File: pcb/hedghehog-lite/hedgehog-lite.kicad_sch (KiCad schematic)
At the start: 31 parts, among them J1 Conn_01x04, J2 AVR-ISP-6, SW1 Reset, SW2 HWB, U1 ATmega32U4-M, Y1 16MHz

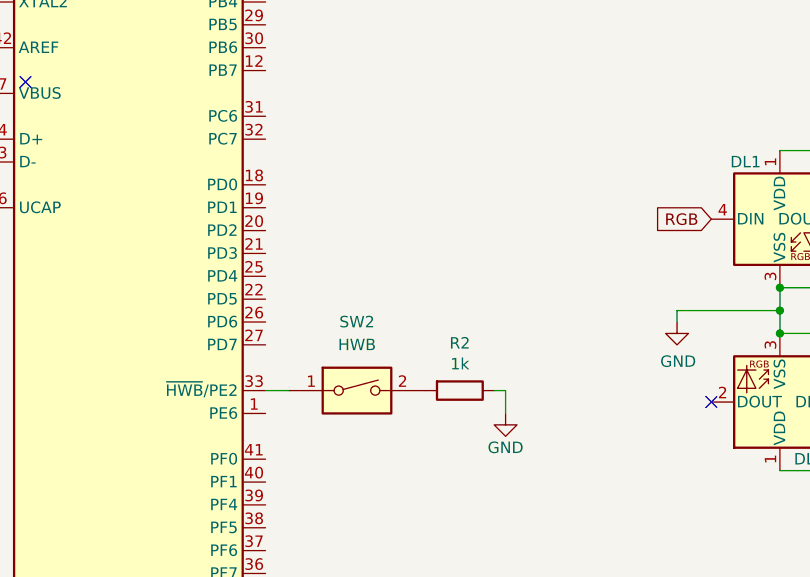
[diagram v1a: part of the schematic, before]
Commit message: Placed all components on PCB
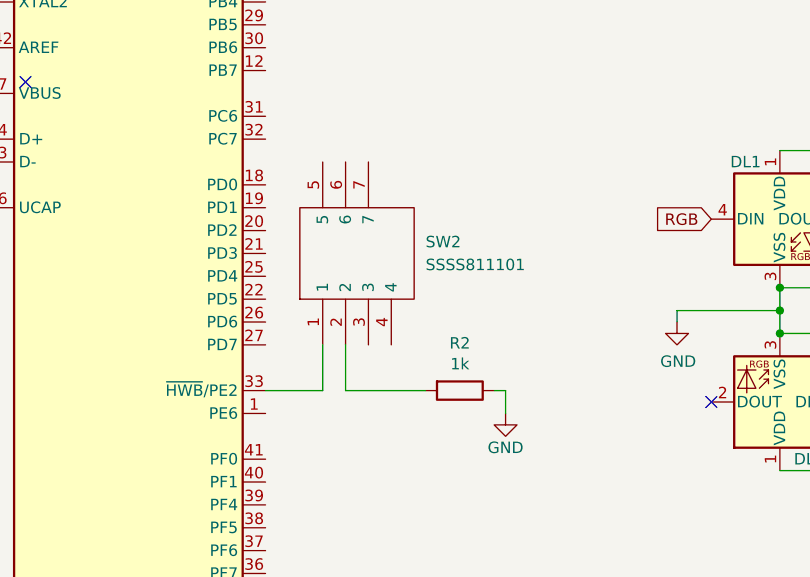
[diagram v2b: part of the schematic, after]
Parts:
- removed SW2: HWB, Button_Switch_SMD:SW_DIP_SPSTx01_Slide_6.7x4.1mm_W8.61mm_P2.54mm_LowProfile, symbol Switch:SW_DIP_x01
- added SW2: SSSS811101, SSSS811101:SSSS811101, symbol SSSS811101:SSSS811101
- DL1, DL10, DL11, DL12, DL13, DL14, DL15, DL2, DL3, DL4, DL5, DL6, DL7, DL8, DL9: LCSC Part # (none) -> C2874885
- J1: LCSC Part # (none) -> C160404
- U1: LCSC Part # (none) -> C112161
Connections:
- net at U1.33 (~{HWB}/PE2): now also SW2.1
- net at R2.2: now also SW2.2

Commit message: Wiring up all parts, excluding matrix
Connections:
- net +5V: no longer DL10.1 (VDD), DL11.1 (VDD), DL12.1 (VDD), DL13.1 (VDD), DL14.1 (VDD), DL15.1 (VDD), DL8.1 (VDD), DL9.1 (VDD)
- net LED_PWR_P: now also DL10.1 (VDD), DL11.1 (VDD), DL12.1 (VDD), DL13.1 (VDD), DL14.1 (VDD), DL15.1 (VDD), DL8.1 (VDD), DL9.1 (VDD)
- net RGB: now also U1.41 (PF0)
- no-connect marks 3 -> 8
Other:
- note added: "Underglow LEDs can be added or left without power. Leave them off during initial flash to reduce ISP current"
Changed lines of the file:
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@@
   (junction (at 77.47 73.66) (diameter 0) (color 0 0 0 0)
   )
+  (no_connect (at 92.71 86.36))
+  (no_connect (at 106.68 134.62))
+  (no_connect (at 104.14 114.3))
+  (no_connect (at 101.6 114.3))
+  (no_connect (at 104.14 134.62))
   (no_connect (at 62.23 101.6))
-  (no_connect (at 66.04 105.41))
+  (no_connect (at 99.06 114.3))
   (no_connect (at 142.24 140.97))
   (wire (pts (xy 256.54 21.59) (xy 264.16 21.59))
@@
     (stroke (width 0) (type default) (color 0 0 0 0))
   )
+  (polyline (pts (xy 217.17 48.26) (xy 278.13 48.26))
+    (stroke (width 0) (type default) (color 0 0 0 0))
+  )
   (wire (pts (xy 46.99 39.37) (xy 57.15 39.37))
     (stroke (width 0) (type default) (color 0 0 0 0))
@@
     (stroke (width 0) (type default) (color 0 0 0 0))
   )
+  (polyline (pts (xy 217.17 48.26) (xy 217.17 57.15))
+    (stroke (width 0) (type default) (color 0 0 0 0))
+  )
   (wire (pts (xy 180.34 128.27) (xy 195.58 128.27))
     (stroke (width 0) (type default) (color 0 0 0 0))
@@
     (stroke (width 0) (type default) (color 0 0 0 0))
   )
+  (wire (pts (xy 92.71 147.32) (xy 101.6 147.32))
+    (stroke (width 0) (type default) (color 0 0 0 0))
+  )
   (wire (pts (xy 149.86 130.81) (xy 138.43 130.81))
     (stroke (width 0) (type default) (color 0 0 0 0))
@@
     (stroke (width 0) (type default) (color 0 0 0 0))
   )
+  (polyline (pts (xy 278.13 48.26) (xy 278.13 57.15))
+    (stroke (width 0) (type default) (color 0 0 0 0))
+  )
   (wire (pts (xy 259.08 25.4) (xy 264.16 25.4))
     (stroke (width 0) (type default) (color 0 0 0 0))
@@
     (stroke (width 0) (type default) (color 0 0 0 0))
   )
+  (polyline (pts (xy 278.13 57.15) (xy 217.17 57.15))
+    (stroke (width 0) (type default) (color 0 0 0 0))
+  )
   (wire (pts (xy 241.3 148.59) (xy 256.54 148.59))
     (stroke (width 0) (type default) (color 0 0 0 0))
@@
   (wire (pts (xy 46.99 35.56) (xy 46.99 39.37))
     (stroke (width 0) (type default) (color 0 0 0 0))
+  )
+  (text "Underglow LEDs can be added or left without power. Leave\nthem off during initial flash to reduce ISP current"
+    (at 218.44 53.34 0)
+    (effects (font (size 1.27 1.27)) (justify left bottom))
   )
   (global_label "SCK" (shape input) (at 100.33 88.9 0) (fields_autoplaced)
@@
     )
   )
-  (global_label "LED_PWR_P" (shape input) (at 187.96 105.41 90) (fields_autoplaced)
+  (global_label "LED_PWR_P" (shape input) (at 187.96 105.41 0) (fields_autoplaced)
     (effects (font (size 1.27 1.27)) (justify left))
-    (property "Intersheet References" "${INTERSHEET_REFS}" (id 0) (at 187.8806 92.3531 90)
+    (property "Intersheet References" "${INTERSHEET_REFS}" (id 0) (at 201.0169 105.3306 0)
+      (effects (font (size 1.27 1.27)) (justify left) hide)
+    )
+  )
+  (global_label "LED_PWR_P" (shape input) (at 203.2 152.4 0) (fields_autoplaced)
+    (effects (font (size 1.27 1.27)) (justify left))
+    (property "Intersheet References" "${INTERSHEET_REFS}" (id 0) (at 216.2569 152.3206 0)
       (effects (font (size 1.27 1.27)) (justify left) hide)
     )
@@
     (property "Intersheet References" "${INTERSHEET_REFS}" (id 0) (at 40.7669 111.6806 0)
       (effects (font (size 1.27 1.27)) (justify right) hide)
+    )
+  )
+  (global_label "RGB" (shape input) (at 101.6 147.32 0) (fields_autoplaced)
+    (effects (font (size 1.27 1.27)) (justify left))
+    (property "Intersheet References" "${INTERSHEET_REFS}" (id 0) (at 107.8231 147.3994 0)
+      (effects (font (size 1.27 1.27)) (justify left) hide)
     )
   )
@@
     (pin "3")
     (pin "4")
-  )
-  (symbol (lib_id "power:VCC") (at 203.2 152.4 180) (unit 1)
-    (in_bom yes) (on_board yes)
-    (property "Reference" "#PWR0121" (id 0) (at 203.2 148.59 0)
-      (effects (font (size 1.27 1.27)) hide)
-    )
-    (property "Value" "VCC" (id 1) (at 205.74 153.6699 0)
-      (effects (font (size 1.27 1.27)) (justify right))
-    )
-    (property "Footprint" "" (id 2) (at 203.2 152.4 0)
-      (effects (font (size 1.27 1.27)) hide)
-    )
-    (property "Datasheet" "" (id 3) (at 203.2 152.4 0)
-      (effects (font (size 1.27 1.27)) hide)
-    )
-    (pin "1")
   )
   (symbol (lib_id "LED:WS2812B") (at 241.3 120.65 0) (unit 1)
@@
     (pin "1")
   )
-  (sheet (at 139.7 59.69) (size 93.98 29.21) (fields_autoplaced)
+  (sheet (at 113.03 55.88) (size 93.98 29.21) (fields_autoplaced)
     (stroke (width 0.1524) (type solid) (color 0 0 0 0))
     (fill (color 0 0 0 0.0000))
-    (property "Sheet name" "Switch Matrix" (id 0) (at 139.7 58.9784 0)
+    (property "Sheet name" "Switch Matrix" (id 0) (at 113.03 55.1684 0)
       (effects (font (size 1.27 1.27)) (justify left bottom))
     )
-    (property "Sheet file" "sw_matrix.kicad_sch" (id 1) (at 139.7 89.4846 0)
+    (property "Sheet file" "sw_matrix.kicad_sch" (id 1) (at 113.03 85.6746 0)
       (effects (font (size 1.27 1.27)) (justify left top))
     )
@@
       (reference "#PWR0120") (unit 1) (value "GND") (footprint "")
     )
-    (path "/7712bc7a-4dd6-4ab1-86d1-22dc5a419cde"
-      (reference "#PWR0121") (unit 1) (value "VCC") (footprint "")
-    )
     (path "/421acd2a-e010-4147-aed0-31f70fcce876"

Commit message: all done but switches
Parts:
- added R3, R4: 22, Resistor_SMD:R_0805_2012Metric, symbol bakeneko-60-pcb-rescue:R-Device
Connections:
- net DN: now also R4.2; no longer U1.3 (D-)
- net DP: now also R3.2; no longer U1.4 (D+)
- new net: R3.1, U1.4 (D+)
- new net: R4.1, U1.3 (D-)
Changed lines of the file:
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@@
   (junction (at 153.67 26.67) (diameter 0) (color 0 0 0 0)
-  )
-  (junction (at 243.84 21.59) (diameter 0) (color 0 0 0 0)
   )
   (junction (at 165.1 148.59) (diameter 0) (color 0 0 0 0)
@@
     (stroke (width 0) (type default) (color 0 0 0 0))
   )
-  (wire (pts (xy 238.76 21.59) (xy 243.84 21.59))
+  (wire (pts (xy 238.76 21.59) (xy 248.92 21.59))
     (stroke (width 0) (type default) (color 0 0 0 0))
   )
@@
     (stroke (width 0) (type default) (color 0 0 0 0))
   )
+  (wire (pts (xy 34.29 110.49) (xy 38.1 110.49))
+    (stroke (width 0) (type default) (color 0 0 0 0))
+  )
   (polyline (pts (xy 217.17 48.26) (xy 278.13 48.26))
     (stroke (width 0) (type default) (color 0 0 0 0))
@@
     (stroke (width 0) (type default) (color 0 0 0 0))
   )
+  (wire (pts (xy 34.29 114.3) (xy 38.1 114.3))
+    (stroke (width 0) (type default) (color 0 0 0 0))
+  )
   (wire (pts (xy 99.06 139.7) (xy 99.06 134.62))
     (stroke (width 0) (type default) (color 0 0 0 0))
@@
     (stroke (width 0) (type default) (color 0 0 0 0))
   )
+  (wire (pts (xy 45.72 110.49) (xy 45.72 111.76))
+    (stroke (width 0) (type default) (color 0 0 0 0))
+  )
   (wire (pts (xy 119.38 142.24) (xy 119.38 139.7))
     (stroke (width 0) (type default) (color 0 0 0 0))
@@
   )
   (wire (pts (xy 36.83 24.13) (xy 46.99 24.13))
-    (stroke (width 0) (type default) (color 0 0 0 0))
-  )
-  (wire (pts (xy 243.84 21.59) (xy 248.92 21.59))
     (stroke (width 0) (type default) (color 0 0 0 0))
   )
@@
     )
   )
-  (global_label "DN" (shape input) (at 45.72 114.3 180) (fields_autoplaced)
+  (global_label "DN" (shape input) (at 34.29 114.3 180) (fields_autoplaced)
     (effects (font (size 1.27 1.27)) (justify right))
-    (property "Intersheet References" "${INTERSHEET_REFS}" (id 0) (at 40.7064 114.2206 0)
+    (property "Intersheet References" "${INTERSHEET_REFS}" (id 0) (at 29.2764 114.2206 0)
       (effects (font (size 1.27 1.27)) (justify right) hide)
     )
@@
     )
   )
-  (global_label "DP" (shape input) (at 45.72 111.76 180) (fields_autoplaced)
+  (global_label "DP" (shape input) (at 34.29 110.49 180) (fields_autoplaced)
     (effects (font (size 1.27 1.27)) (justify right))
-    (property "Intersheet References" "${INTERSHEET_REFS}" (id 0) (at 40.7669 111.6806 0)
+    (property "Intersheet References" "${INTERSHEET_REFS}" (id 0) (at 29.3369 110.4106 0)
       (effects (font (size 1.27 1.27)) (justify right) hide)
     )
@@
     (pin "1")
   )
+  (symbol (lib_id "bakeneko-60-pcb-rescue:R-Device") (at 41.91 110.49 270) (unit 1)
+    (in_bom yes) (on_board yes)
+    (property "Reference" "R3" (id 0) (at 41.91 108.585 90))
+    (property "Value" "22" (id 1) (at 41.91 110.49 90))
+    (property "Footprint" "Resistor_SMD:R_0805_2012Metric" (id 2) (at 41.91 108.712 90)
+      (effects (font (size 1.27 1.27)) hide)
+    )
+    (property "Datasheet" "~" (id 3) (at 41.91 110.49 0)
+      (effects (font (size 1.27 1.27)) hide)
+    )
+    (property "LCSC Part #" "C17561" (id 4) (at 41.91 110.49 0)
+      (effects (font (size 1.27 1.27)) hide)
+    )
+    (pin "1")
+    (pin "2")
+  )
   (symbol (lib_id "bakeneko-60-pcb-rescue:Crystal_GND24-Device") (at 95.25 31.75 90) (unit 1)
     (in_bom yes) (on_board yes)
@@
     )
     (property "LCSC Part #" "C15850" (id 4) (at 57.15 31.75 0)
+      (effects (font (size 1.27 1.27)) hide)
+    )
+    (pin "1")
+    (pin "2")
+  )
+  (symbol (lib_id "bakeneko-60-pcb-rescue:R-Device") (at 41.91 114.3 270) (unit 1)
+    (in_bom yes) (on_board yes)
+    (property "Reference" "R4" (id 0) (at 41.91 112.395 90))
+    (property "Value" "22" (id 1) (at 41.91 114.3 90))
+    (property "Footprint" "Resistor_SMD:R_0805_2012Metric" (id 2) (at 41.91 112.522 90)
+      (effects (font (size 1.27 1.27)) hide)
+    )
+    (property "Datasheet" "~" (id 3) (at 41.91 114.3 0)
+      (effects (font (size 1.27 1.27)) hide)
+    )
+    (property "LCSC Part #" "C17561" (id 4) (at 41.91 114.3 0)
       (effects (font (size 1.27 1.27)) hide)
     )
@@
     (pin "2")
   )
-  (symbol (lib_id "power:VBUS") (at 256.54 21.59 0) (unit 1)
-    (in_bom yes) (on_board yes) (fields_autoplaced)
-    (property "Reference" "#PWR0114" (id 0) (at 256.54 25.4 0)
-      (effects (font (size 1.27 1.27)) hide)
-    )
-    (property "Value" "VBUS" (id 1) (at 256.54 16.51 0))
-    (property "Footprint" "" (id 2) (at 256.54 21.59 0)
-      (effects (font (size 1.27 1.27)) hide)
-    )
-    (property "Datasheet" "" (id 3) (at 256.54 21.59 0)
-      (effects (font (size 1.27 1.27)) hide)
-    )
-    (pin "1")
-  )
   (symbol (lib_id "Connector_Generic:Conn_01x04") (at 269.24 25.4 0) (unit 1)
     (in_bom yes) (on_board yes) (fields_autoplaced)
@@
     (pin "1")
   )
-  (symbol (lib_id "power:VBUS") (at 243.84 21.59 0) (unit 1)
-    (in_bom yes) (on_board yes) (fields_autoplaced)
-    (property "Reference" "#PWR0112" (id 0) (at 243.84 25.4 0)
-      (effects (font (size 1.27 1.27)) hide)
-    )
-    (property "Value" "VBUS" (id 1) (at 243.84 16.51 0))
-    (property "Footprint" "" (id 2) (at 243.84 21.59 0)
-      (effects (font (size 1.27 1.27)) hide)
-    )
-    (property "Datasheet" "" (id 3) (at 243.84 21.59 0)
-      (effects (font (size 1.27 1.27)) hide)
-    )
-    (pin "1")
-  )
   (symbol (lib_id "LED:WS2812B") (at 256.54 140.97 180) (unit 1)
     (in_bom yes) (on_board yes)
@@
     (pin "3")
     (pin "4")
+  )
+  (symbol (lib_id "power:VCC") (at 256.54 21.59 0) (unit 1)
+    (in_bom yes) (on_board yes)
+    (property "Reference" "#PWR0112" (id 0) (at 256.54 25.4 0)
+      (effects (font (size 1.27 1.27)) hide)
+    )
+    (property "Value" "VCC" (id 1) (at 256.54 16.51 0))
+    (property "Footprint" "" (id 2) (at 256.54 21.59 0)
+      (effects (font (size 1.27 1.27)) hide)
+    )
+    (property "Datasheet" "" (id 3) (at 256.54 21.59 0)
+      (effects (font (size 1.27 1.27)) hide)
+    )
+    (pin "1")
   )
   (symbol (lib_id "LED:WS2812B") (at 241.3 140.97 180) (unit 1)
@@
     (pin "1")
   )
-  (sheet (at 113.03 55.88) (size 93.98 29.21) (fields_autoplaced)
+  (sheet (at 113.03 57.15) (size 39.37 27.94) (fields_autoplaced)
     (stroke (width 0.1524) (type solid) (color 0 0 0 0))
     (fill (color 0 0 0 0.0000))
-    (property "Sheet name" "Switch Matrix" (id 0) (at 113.03 55.1684 0)
+    (property "Sheet name" "Switch Matrix" (id 0) (at 113.03 56.4384 0)
       (effects (font (size 1.27 1.27)) (justify left bottom))
     )
@@
       (reference "#PWR0111") (unit 1) (value "VCC") (footprint "")
     )
-    (path "/a993c56f-11f6-4404-bd64-e97c4f8902c7"
-      (reference "#PWR0112") (unit 1) (value "VBUS") (footprint "")
+    (path "/dad34091-c7fa-46ac-8890-1f6569d146a1"
+      (reference "#PWR0112") (unit 1) (value "VCC") (footprint "")
     )
     (path "/38bc573d-ed33-43d3-b37e-dbdc7be602cb"
       (reference "#PWR0113") (unit 1) (value "+5V") (footprint "")
     )
-    (path "/979634cd-c88e-45a9-a703-4310b6d115d4"
-      (reference "#PWR0114") (unit 1) (value "VBUS") (footprint "")
-    )
     (path "/01fd36cd-ab93-4199-8230-8fb99caf37eb"
       (reference "#PWR0115") (unit 1) (value "GND") (footprint "")
@@
       (reference "R2") (unit 1) (value "1k") (footprint "Resistor_SMD:R_0805_2012Metric")
     )
+    (path "/05a81e37-5594-40fc-87e2-da722e3f2494"
+      (reference "R3") (unit 1) (value "22") (footprint "Resistor_SMD:R_0805_2012Metric")
+    )
+    (path "/0f3ac837-3bca-48c4-bd0e-be5d15e21d99"
+      (reference "R4") (unit 1) (value "22") (footprint "Resistor_SMD:R_0805_2012Metric")
+    )
     (path "/ea0d715a-bc39-428e-b536-93445699f1d7"

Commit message: Top Row done
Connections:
- net SCK renamed ROW8
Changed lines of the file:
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@@
   (junction (at 210.82 128.27) (diameter 0) (color 0 0 0 0)
   )
+  (junction (at 97.79 88.9) (diameter 0) (color 0 0 0 0)
+  )
   (junction (at 210.82 113.03) (diameter 0) (color 0 0 0 0)
   )
@@
   )
   (junction (at 74.93 172.72) (diameter 0) (color 0 0 0 0)
+  )
+  (junction (at 98.425 98.425) (diameter 0) (color 0 0 0 0)
   )
   (junction (at 149.86 130.81) (diameter 0) (color 0 0 0 0)
@@
     (stroke (width 0) (type default) (color 0 0 0 0))
   )
+  (wire (pts (xy 98.425 98.425) (xy 99.695 98.425))
+    (stroke (width 0) (type default) (color 0 0 0 0))
+  )
   (wire (pts (xy 195.58 128.27) (xy 210.82 128.27))
     (stroke (width 0) (type default) (color 0 0 0 0))
@@
     (stroke (width 0) (type default) (color 0 0 0 0))
   )
+  (wire (pts (xy 97.79 86.995) (xy 97.79 88.9))
+    (stroke (width 0) (type default) (color 0 0 0 0))
+  )
   (wire (pts (xy 226.06 128.27) (xy 241.3 128.27))
     (stroke (width 0) (type default) (color 0 0 0 0))
@@
     (stroke (width 0) (type default) (color 0 0 0 0))
   )
+  (wire (pts (xy 98.425 98.425) (xy 98.425 100.33))
+    (stroke (width 0) (type default) (color 0 0 0 0))
+  )
   (wire (pts (xy 77.47 73.66) (xy 77.47 78.74))
     (stroke (width 0) (type default) (color 0 0 0 0))
   )
+  (wire (pts (xy 98.425 93.98) (xy 98.425 98.425))
+    (stroke (width 0) (type default) (color 0 0 0 0))
+  )
   (wire (pts (xy 43.18 105.41) (xy 43.18 106.68))
     (stroke (width 0) (type default) (color 0 0 0 0))
@@
     (stroke (width 0) (type default) (color 0 0 0 0))
   )
-  (wire (pts (xy 92.71 88.9) (xy 100.33 88.9))
+  (wire (pts (xy 106.045 93.345) (xy 100.33 93.345))
+    (stroke (width 0) (type default) (color 0 0 0 0))
+  )
+  (wire (pts (xy 92.71 88.9) (xy 97.79 88.9))
     (stroke (width 0) (type default) (color 0 0 0 0))
   )
@@
     (stroke (width 0) (type default) (color 0 0 0 0))
   )
+  (wire (pts (xy 97.79 88.9) (xy 100.33 88.9))
+    (stroke (width 0) (type default) (color 0 0 0 0))
+  )
   (wire (pts (xy 187.96 113.03) (xy 195.58 113.03))
     (stroke (width 0) (type default) (color 0 0 0 0))
@@
     (stroke (width 0) (type default) (color 0 0 0 0))
   )
-  (wire (pts (xy 92.71 93.98) (xy 100.33 93.98))
-    (stroke (width 0) (type default) (color 0 0 0 0))
-  )
   (wire (pts (xy 180.34 113.03) (xy 187.96 113.03))
     (stroke (width 0) (type default) (color 0 0 0 0))
@@
     (stroke (width 0) (type default) (color 0 0 0 0))
   )
+  (wire (pts (xy 100.33 93.345) (xy 100.33 91.44))
+    (stroke (width 0) (type default) (color 0 0 0 0))
+  )
   (wire (pts (xy 48.26 96.52) (xy 62.23 96.52))
     (stroke (width 0) (type default) (color 0 0 0 0))
@@
   )
   (wire (pts (xy 138.43 26.67) (xy 142.24 26.67))
+    (stroke (width 0) (type default) (color 0 0 0 0))
+  )
+  (wire (pts (xy 92.71 93.98) (xy 98.425 93.98))
     (stroke (width 0) (type default) (color 0 0 0 0))
   )
@@
     )
   )
-  (global_label "MOSI" (shape input) (at 100.33 91.44 0) (fields_autoplaced)
-    (effects (font (size 1.27 1.27)) (justify left))
-    (property "Intersheet References" "${INTERSHEET_REFS}" (id 0) (at 19.05 -6.35 0)
+  (global_label "MOSI" (shape input) (at 106.045 93.345 0) (fields_autoplaced)
+    (effects (font (size 1.27 1.27)) (justify left))
+    (property "Intersheet References" "${INTERSHEET_REFS}" (id 0) (at 24.765 -4.445 0)
       (effects (font (size 1.27 1.27)) hide)
     )
@@
     )
   )
-  (global_label "MISO" (shape input) (at 100.33 93.98 0) (fields_autoplaced)
-    (effects (font (size 1.27 1.27)) (justify left))
-    (property "Intersheet References" "${INTERSHEET_REFS}" (id 0) (at 19.05 -6.35 0)
+  (global_label "MISO" (shape input) (at 98.425 100.33 270) (fields_autoplaced)
+    (effects (font (size 1.27 1.27)) (justify right))
+    (property "Intersheet References" "${INTERSHEET_REFS}" (id 0) (at 198.755 19.05 0)
       (effects (font (size 1.27 1.27)) hide)
     )
@@
     )
   )
+  (global_label "ROW8" (shape input) (at 97.79 86.995 90) (fields_autoplaced)
+    (effects (font (size 1.27 1.27)) (justify left))
+    (property "Intersheet References" "${INTERSHEET_REFS}" (id 0) (at 97.7106 79.3205 90)
+      (effects (font (size 1.27 1.27)) (justify left) hide)
+    )
+  )
   (global_label "SCK" (shape input) (at 203.2 34.29 0) (fields_autoplaced)
     (effects (font (size 1.27 1.27)) (justify left))
@@
     )
   )
+  (global_label "ROW0" (shape input) (at 99.695 98.425 0) (fields_autoplaced)
+    (effects (font (size 1.27 1.27)) (justify left))
+    (property "Intersheet References" "${INTERSHEET_REFS}" (id 0) (at 107.3695 98.3456 0)
+      (effects (font (size 1.27 1.27)) (justify left) hide)
+    )
+  )

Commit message: All routing done
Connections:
- net COL8: now reaches U1.18 (PD0)
- net ROW1: now reaches U1.19 (PD1)
- net ROW2: now reaches U1.20 (PD2)
- net ROW6: now reaches U1.21 (PD3)
- net ROW7: now reaches U1.22 (PD5)
- net COL5: now reaches U1.25 (PD4)
- net COL6: now reaches U1.26 (PD6)
- net COL7: now reaches U1.27 (PD7)
- net ROW4: now reaches U1.28 (PB4)
- net ROW5: now reaches U1.29 (PB5)
- net COL4: now reaches U1.36 (PF7)
- net COL3: now reaches U1.37 (PF6)
- net COL2: now reaches U1.38 (PF5)
- net COL1: now reaches U1.39 (PF4)
- net ROW3: now reaches U1.40 (PF1)
- net MOSI renamed COL0
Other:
- moved on the sheet: R2, SW2
